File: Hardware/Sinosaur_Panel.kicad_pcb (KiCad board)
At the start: 2 copper layers, 60.8 x 128.5 mm, 31 parts

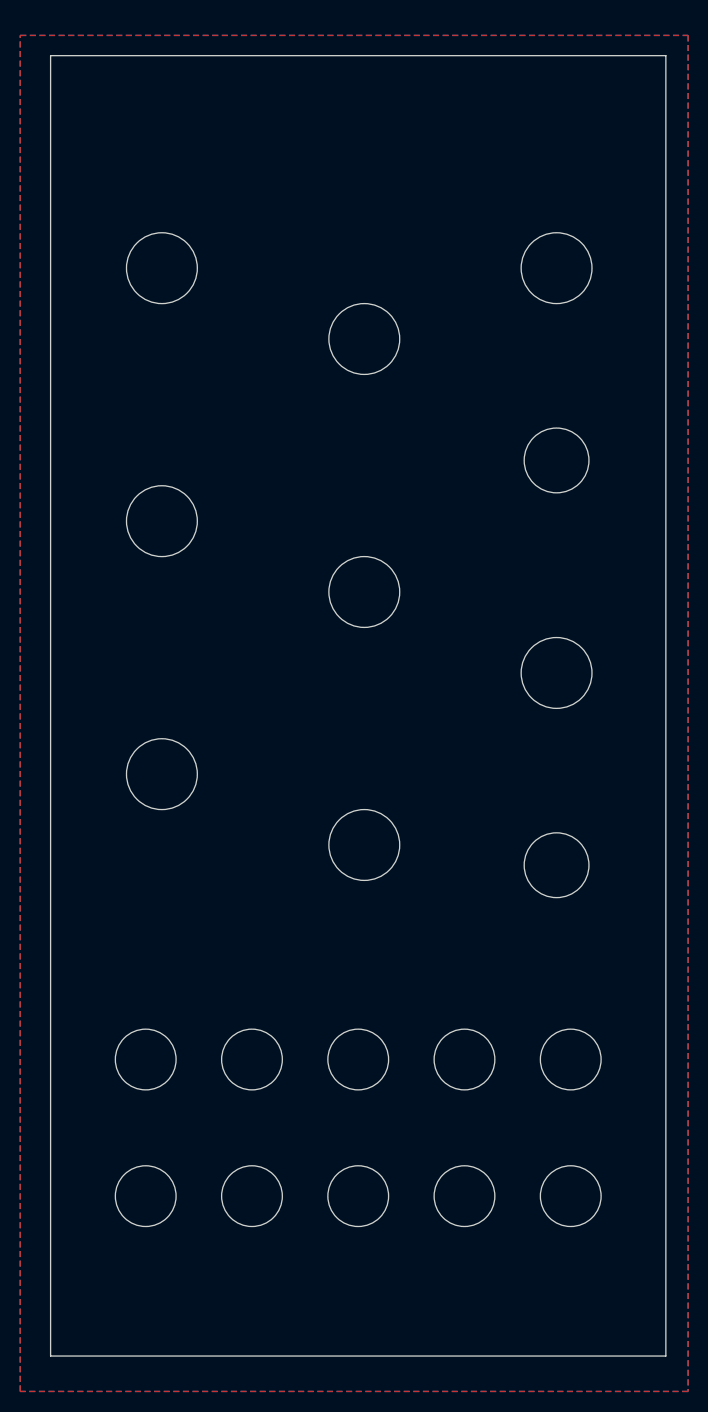
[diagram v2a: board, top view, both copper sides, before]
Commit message: Control PCB wiring
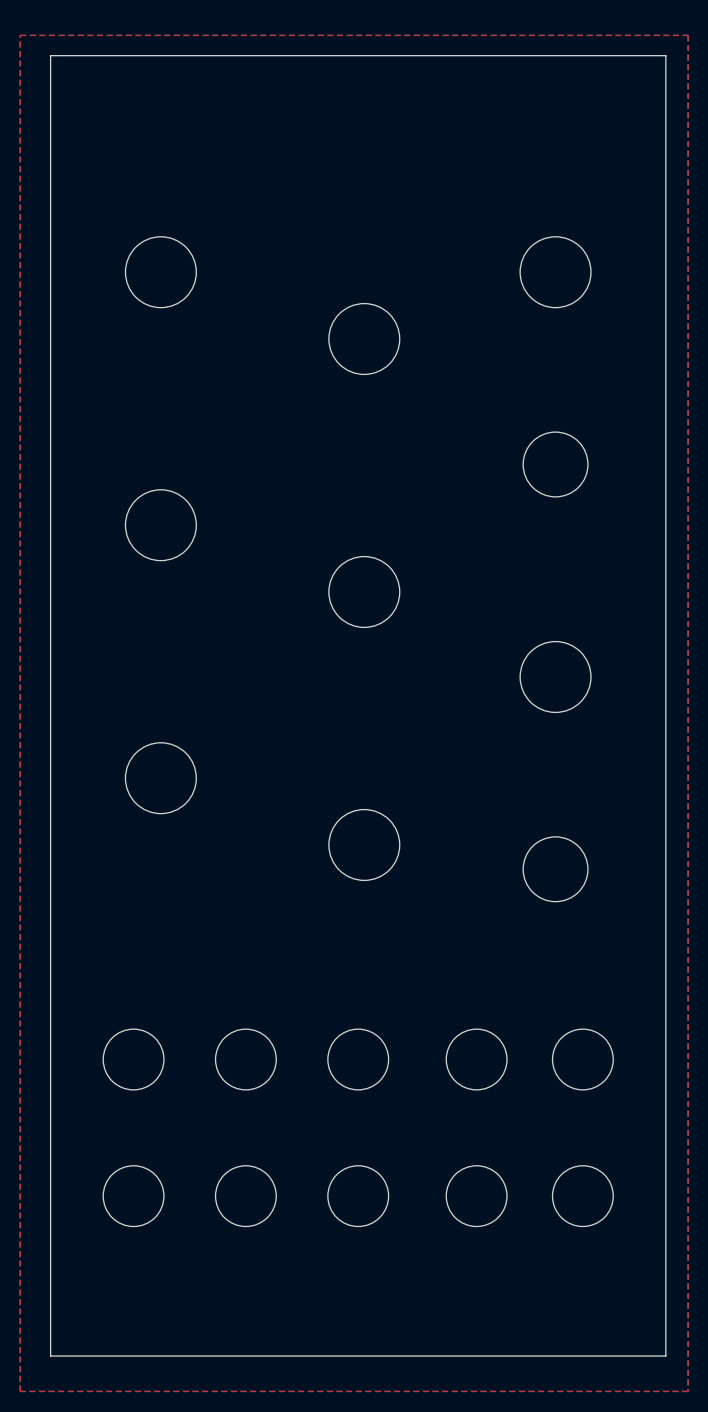
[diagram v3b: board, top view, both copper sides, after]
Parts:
- moved kibuzzard-666C2AB0 1.90 mm to (101.5, 62.2)
- moved kibuzzard-666C2AB5 1.90 mm to (101.5, 87.2)
- moved kibuzzard-666C2ABA 1.90 mm to (101.5, 112.2)
- moved Ref** 1.20 mm to (107.8, 140.0)
- moved Ref** 1.20 mm to (107.8, 153.5)
- moved kibuzzard-666C296D 1.20 mm to (107.8, 147.0)
- moved Ref** 1.20 mm to (152.2, 153.5)
- moved Ref** 1.20 mm to (152.2, 140.0)
- moved Ref** 1.20 mm to (141.7, 140.0)
- moved Ref** 1.20 mm to (141.7, 153.5)
- moved Ref** 0.60 mm to (118.9, 153.5)
- moved Ref** 0.60 mm to (118.9, 140.0)
- moved kibuzzard-666C29A3 0.60 mm to (118.9, 146.7)
- moved Ref** 0.41 mm to (149.5, 102.2)
- moved Ref** 0.41 mm to (149.5, 62.2)
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
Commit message: Gerber production
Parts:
- moved G*** 1.88 mm to (130.0, 46.6)

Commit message: Gerber production for v1
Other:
- board text added: "Clock"
- board text added: "Gate"
- board text removed: "CLK"
- board text removed: "GATE"
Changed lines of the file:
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@@
 		(layer "B.SilkS")
+	)
+	(gr_line
+		(start 102.9 160.6)
+		(end 114.6 160.6)
+		(stroke
+			(width 0.5)
+			(type default)
+		)
+		(layer "F.Mask")
 	)
 	(gr_rect
@@
 		(layer "F.Mask")
 	)
+	(gr_line
+		(start 123.1 160.6)
+		(end 134.7 160.6)
+		(stroke
+			(width 0.5)
+			(type default)
+		)
+		(layer "F.Mask")
+	)
 	(gr_circle
 		(center 120.5 65.6)
@@
 		)
 	)
-	(gr_text "GATE"
-		(at 151 134.778175 0)
+	(gr_text "Gate"
+		(at 152.2 134.5 0)
 		(layer "F.Mask")
 		(effects
@@
 	)
 	(gr_text "Sine"
-		(at 118.4 161.778175 0)
+		(at 118.9 161.778175 0)
 		(layer "F.Mask")
 		(effects
@@
 		)
 	)
-	(gr_text "CLK"
-		(at 140.5 134.778175 0)
-		(layer "F.Mask")
-		(effects
+	(gr_text "Clock"
+		(at 141.7 134.5 0)
+		(layer "F.Mask")
+		(effects

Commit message: Ramp and swell pots exponentially scaled for better control at low values
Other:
- board text added: "Mountjoy Modular 2024 Sinosaur Panel v2.0"
- board text removed: "Mountjoy Modular 2024 Sinosaur Panel v1.0"
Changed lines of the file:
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@@
 		)
 	)
-	(gr_text "Mountjoy Modular 2024\nSinosaur Panel v1.0"
+	(gr_text "Mountjoy Modular 2024\nSinosaur Panel v2.0"
 		(at 129.8 44.5 0)
 		(layer "B.SilkS")
